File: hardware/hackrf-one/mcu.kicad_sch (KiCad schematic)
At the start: 132 parts, among them J1 USB-MICRO-B, P1 1V8, P20 GPIO, P22 I2S, P23 DBGEN, P24 TRST, P25 LPC_ISP, P26 LPC_JTAG, P28 SD, P29 CPLD_JTAG, P3 GND, P30 BANK2_AUX, P5 LEDS, P68 SPIFI_CS, P69 VREGMODE, P70 EN_1V8, P71 ID, P72 GP_CLKIN, P73 P1_2, P74 P1_1, P75 GP_CLKIN, P76 GP_CLKIN, P77 GP_CLKIN, P78 GP_CLKIN, P79 GP_CLKIN, P8 VCC, P80 SHIELD, P81 SPIFI_SIO2, P82 SPIFI_SIO3, Q5 MOSFET_P, SW1 DFU, SW2 RESET, U15 USB6B1, U20 W25Q80, U21 TPS62410, U23 LPC4320FBD144, U24 GSG-XC2C64A-7VQG100C, X2 MCU_XTAL, X3 RTC_XTAL

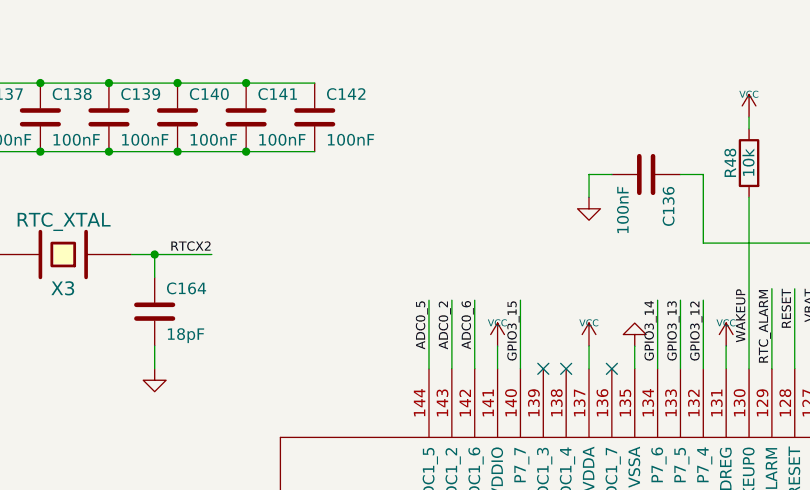
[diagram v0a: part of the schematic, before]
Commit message: mcu: add power flags
Add flags to the power nets to mark them as such.

Signed-off-by: Sean Cross <sean@xobs.io>
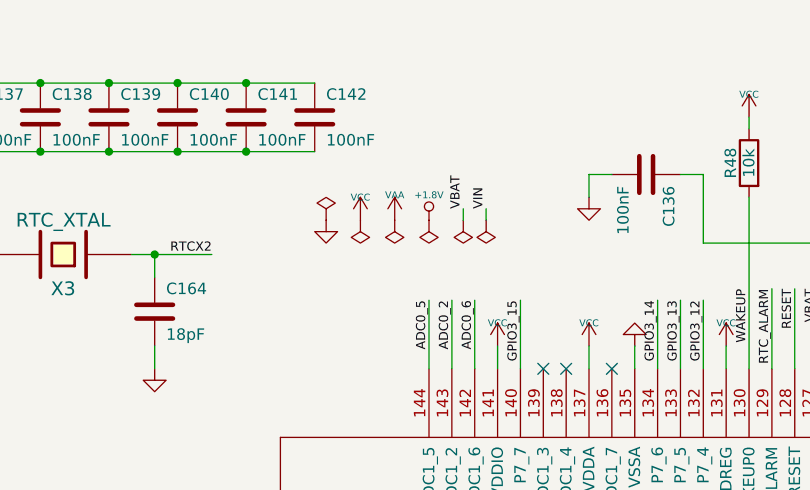
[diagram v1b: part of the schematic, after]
